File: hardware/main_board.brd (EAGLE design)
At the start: 91.4 x 66 mm, 108 parts, among them IC1 IC_USBLC6-2, IC2 LM1117IMPX-3.3, IC3 STM32F107RCT, IC4 DP83848, IC5 LM1117MPX-2.5, U1 USD-SOCKETUSD, U2 VS1003, X2 CRYSTALS-NOGND-CFPX-217, X3 KUSBVX, Y1 CRYSTAL-GROUNDEDSMD-5X3.2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

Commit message: minor changes
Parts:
- removed SV1: (no value), con-harting-ml:ML14L
- added SV2: (no value), con-harting-ml:ML10L
- moved C27 5.12 mm to (43.9, 10.8)
- moved C5 5.12 mm to (43.3, 8.92)
- moved IC1 5.12 mm to (48.3, 16.7)
- moved X3 5.12 mm to (48.3, 12.7)
- moved JP2 0.89 mm to (58.8, 6.39)
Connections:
- new net PA10: IC3.43, SV2.10
- new net PA8: IC3.41, SV2.8
- new net PA9: IC3.42, SV2.9
- new net PB14: IC3.35, SV2.2
- new net PB15: IC3.36, SV2.3
- new net PC6: IC3.37, SV2.4
- new net PC7: IC3.38, SV2.5
- new net PC8: IC3.39, SV2.6
- new net PC9: IC3.40, SV2.7
- net 3V: no longer SV1.1, SV1.2
- net GND: now also SV2.1; no longer SV1.3, SV1.4
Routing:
- net PB14: track 0.00 -> 19.0 mm
- net PC6: track 0.00 -> 18.3 mm
- net PC8: track 0.00 -> 17.7 mm
- net PA8: track 0.00 -> 17.0 mm
- net PA10: track 0.00 -> 16.4 mm
- net PB15: track 0.00 -> 15.6 mm
- net PC7: track 0.00 -> 14.9 mm
- net PC9: track 0.00 -> 14.3 mm
- net PA9: track 0.00 -> 13.7 mm
- net USB_P: track 8.27 -> 11.9 mm
- net USB_N: track 8.27 -> 11.9 mm
- net VBUS: track 89.9 -> 88.4 mm
- net 3V: track 442.8 -> 444.1 mm
- net SWD_CLK: track 29.5 -> 30.4 mm
- net NRST: track 56.0 -> 56.9 mm
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
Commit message: Minor changes
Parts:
- added C6: (no value), rcl:C0603
- added JP3: (no value), pinhead:1X02/90
- added R12: (no value), rcl:R0603
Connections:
- net 3V: now also JP3.1, R12.2
- net GND: now also C6.2, JP3.2
- net NRST: now also C6.1, R12.1
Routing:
- net 3V: track 444.1 -> 447.3 mm
- net NRST: track 56.9 -> 59.7 mm
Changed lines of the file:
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@@
 <setting verticaltext="up"/>
 </settings>
-<grid distance="25" unitdist="mil" unit="mil" style="lines" multiple="1" display="no" altdistance="1" altunitdist="mil" altunit="mil"/>
+<grid distance="25" unitdist="mil" unit="mil" style="lines" multiple="1" display="no" altdistance="5" altunitdist="mil" altunit="mil"/>
 <layers>
 <layer number="1" name="Top" color="4" fill="1" visible="yes" active="yes"/>
@@
 <attribute name="MF" value="" x="32.7406" y="10.795" size="1.778" layer="28" rot="MR180" display="off"/>
 </element>
+<element name="JP3" library="pinhead" package="1X02/90" value="" x="14.896221875" y="6.35" rot="MR180"/>
+<element name="R12" library="rcl" package="R0603" value="" x="50.8508" y="6.3872" rot="R180"/>
+<element name="C6" library="rcl" package="C0603" value="" x="53.7464" y="10.0584" rot="R90"/>
 </elements>
 <signals>
@@
 <via x="74.1934" y="8.4074" extent="1-16" drill="0.5" diameter="1.4224" shape="octagon"/>
 <wire x1="21.5794" y1="25.1108" x2="21.5794" y2="22.9616" width="0.3048" layer="1"/>
-<via x="6.0854" y="15.2654" extent="1-16" drill="0.6" diameter="1.4224" shape="octagon"/>
+<via x="6.0854" y="14.6304" extent="1-16" drill="0.6" diameter="1.4224" shape="octagon"/>
 <via x="26.2022" y="29.0068" extent="1-16" drill="0.6" diameter="1.4224" shape="octagon"/>
 <wire x1="21.0794" y1="33.4108" x2="21.0794" y2="30.6044" width="0.3048" layer="1"/>
@@
 <contactref element="SV2" pad="1"/>
 <via x="21.9604" y="14.6304" extent="1-16" drill="0.6" diameter="1.4224" shape="octagon"/>
+<contactref element="JP3" pad="2"/>
+<contactref element="C6" pad="2"/>
 </signal>
 <signal name="3V">
@@
 <wire x1="63.9064" y1="6.3872" x2="63.9064" y2="4.2164" width="1.016" layer="1"/>
 <wire x1="63.9064" y1="4.2164" x2="62.865" y2="3.175" width="1.016" layer="1"/>
-<wire x1="62.865" y1="3.175" x2="15.875" y2="3.175" width="1.016" layer="1"/>
+<wire x1="62.865" y1="3.175" x2="50.0008" y2="3.175" width="1.016" layer="1"/>
+<wire x1="50.0008" y1="3.175" x2="15.875" y2="3.175" width="1.016" layer="1"/>
 <wire x1="35.4488" y1="26.0108" x2="33.9598" y2="26.0108" width="0.3048" layer="1"/>
 <wire x1="33.9598" y1="26.0108" x2="33.9598" y2="25.81378125" width="0.3048" layer="1"/>
@@
 <wire x1="33.4614" y1="32.5108" x2="33.4614" y2="32.709090625" width="0.3048" layer="1"/>
 <wire x1="22.4926" y1="21.375" x2="24.0792" y2="22.9616" width="0.4064" layer="16"/>
+<wire x1="13.626221875" y1="5.423778125" x2="15.875" y2="3.175" width="1.016" layer="1"/>
+<contactref element="JP3" pad="1"/>
+<wire x1="13.626221875" y1="10.16" x2="13.626221875" y2="21.375" width="1.016" layer="1"/>
+<wire x1="13.626221875" y1="5.423778125" x2="13.626221875" y2="10.16" width="1.016" layer="1"/>
+<contactref element="R12" pad="2"/>
+<wire x1="50.0008" y1="6.3872" x2="50.0008" y2="3.175" width="0.6096" layer="1"/>
 <wire x1="13.626221875" y1="21.375" x2="22.4926" y2="21.375" width="0.4064" layer="16"/>
-<wire x1="15.875" y1="3.175" x2="13.626221875" y2="5.423778125" width="1.016" layer="1"/>
-<wire x1="13.626221875" y1="21.375" x2="13.626221875" y2="5.423778125" width="1.016" layer="1"/>
 <wire x1="25.5896" y1="41.43501875" x2="25.292559375" y2="41.43501875" width="0" layer="19" extent="1-1"/>
 </signal>
@@
 <contactref element="JP2" pad="5"/>
 <wire x1="58.5216" y1="17.6784" x2="57.1246" y2="19.0754" width="0.3048" layer="1"/>
-<wire x1="53.7464" y1="6.3872" x2="53.7464" y2="8.4328" width="0.3048" layer="1"/>
-<wire x1="53.7464" y1="8.4328" x2="58.5216" y2="13.208" width="0.3048" layer="1"/>
-<wire x1="58.5216" y1="17.6784" x2="58.5216" y2="13.208" width="0.3048" layer="1"/>
+<wire x1="55.03" y1="9.2084" x2="58.5216" y2="12.7" width="0.3048" layer="1"/>
+<wire x1="58.5216" y1="17.6784" x2="58.5216" y2="12.7" width="0.3048" layer="1"/>
 <via x="53.0098" y="19.0754" extent="1-16" drill="0.6" diameter="1.4224" shape="octagon"/>
 <wire x1="57.1246" y1="19.0754" x2="53.0098" y2="19.0754" width="0.3048" layer="1"/>
@@
 <wire x1="41.9488" y1="39.9662" x2="41.148" y2="40.767" width="0.3048" layer="16"/>
 <wire x1="42.8886" y1="31.115" x2="41.9488" y2="32.0548" width="0.3048" layer="16"/>
+<contactref element="R12" pad="1"/>
+<wire x1="51.7008" y1="6.3872" x2="53.7464" y2="6.3872" width="0.6096" layer="1"/>
+<contactref element="C6" pad="1"/>
+<wire x1="53.7464" y1="9.2084" x2="55.03" y2="9.2084" width="0.3048" layer="1"/>
+<wire x1="53.7464" y1="9.2084" x2="53.7464" y2="6.3872" width="0.6096" layer="1"/>
 </signal>
 <signal name="SWD_CLK">

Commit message: Minor changes
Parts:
- moved JP3 1.27 mm to (14.9, 7.62)
- moved R36 0.13 mm to (53.9, 38.5)
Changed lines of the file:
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@@
 <setting verticaltext="up"/>
 </settings>
-<grid distance="25" unitdist="mil" unit="mil" style="lines" multiple="1" display="no" altdistance="5" altunitdist="mil" altunit="mil"/>
+<grid distance="25" unitdist="mil" unit="mil" style="lines" multiple="1" display="no" altdistance="1" altunitdist="mil" altunit="mil"/>
 <layers>
 <layer number="1" name="Top" color="4" fill="1" visible="yes" active="yes"/>
@@
 <element name="L1" library="dp_devices" package="FB805" value="" x="73.025" y="42.291" rot="MR0"/>
 <element name="R35" library="rcl" package="R0603" value="" x="72.52461875" y="27.686"/>
-<element name="R36" library="rcl" package="R0603" value="100k" x="53.9242" y="38.3667" rot="R90"/>
+<element name="R36" library="rcl" package="R0603" value="100k" x="53.9242" y="38.4937" rot="R90"/>
 <element name="L2" library="dp_devices" package="FB805" value="" x="66.675" y="44.6786" rot="R180"/>
 <element name="C56" library="rcl" package="C0603" value="10 uF" x="68.4276" y="32.458659375" rot="R270"/>
@@
 <attribute name="MF" value="" x="32.7406" y="10.795" size="1.778" layer="28" rot="MR180" display="off"/>
 </element>
-<element name="JP3" library="pinhead" package="1X02/90" value="" x="14.896221875" y="6.35" rot="MR180"/>
+<element name="JP3" library="pinhead" package="1X02/90" value="" x="14.896221875" y="7.62" rot="MR180"/>
 <element name="R12" library="rcl" package="R0603" value="" x="50.8508" y="6.3872" rot="R180"/>
 <element name="C6" library="rcl" package="C0603" value="" x="53.7464" y="10.0584" rot="R90"/>
@@
 <via x="52.0192" y="64.516" extent="1-16" drill="0.5" diameter="1.27" shape="octagon"/>
 <via x="21.5794" y="22.9616" extent="1-16" drill="0.6" diameter="1.4224" shape="octagon"/>
-<via x="63.0428" y="36.4998" extent="1-16" drill="0.5" diameter="1.27" shape="octagon"/>
+<via x="63.4238" y="36.6014" extent="1-16" drill="0.5" diameter="1.27" shape="octagon"/>
 <contactref element="U2" pad="4"/>
 <contactref element="U2" pad="22"/>
@@
 <contactref element="IC3" pad="64"/>
 <contactref element="IC3" pad="48"/>
-<via x="61.214" y="36.5506" extent="1-16" drill="0.6" diameter="1.4224" shape="octagon"/>
-<wire x1="61.214" y1="36.5506" x2="61.214" y2="33.308659375" width="1.016" layer="16"/>
+<via x="61.214" y="36.6776" extent="1-16" drill="0.6" diameter="1.4224" shape="octagon"/>
+<wire x1="61.214" y1="36.6776" x2="61.214" y2="33.308659375" width="1.016" layer="16"/>
 <wire x1="44.9488" y1="32.8758" x2="44.9488" y2="26.0108" width="0.3048" layer="1"/>
 <wire x1="44.9488" y1="26.0108" x2="44.9488" y2="24.0108" width="0.3048" layer="1"/>
@@
 <wire x1="64.71181875" y1="40.382" x2="61.591" y2="40.382" width="0.254" layer="1"/>
 <wire x1="61.591" y1="40.382" x2="61.214" y2="40.005" width="0.254" layer="1"/>
-<wire x1="61.214" y1="40.005" x2="61.214" y2="36.5506" width="0.254" layer="1"/>
-<wire x1="61.214" y1="36.5506" x2="52.4764" y2="36.5506" width="0.3048" layer="1"/>
-<wire x1="51.8922" y1="35.9664" x2="52.4764" y2="36.5506" width="0.3048" layer="1"/>
+<wire x1="61.214" y1="40.005" x2="61.214" y2="36.6776" width="0.254" layer="1"/>
+<wire x1="51.8922" y1="35.9664" x2="52.6034" y2="36.6776" width="0.3048" layer="1"/>
 <wire x1="48.80101875" y1="33.5108" x2="48.80101875" y2="33.71111875" width="0.3048" layer="1"/>
 <wire x1="48.80101875" y1="33.5108" x2="51.5194" y2="33.5108" width="0.3048" layer="1"/>
 <wire x1="51.5194" y1="33.5108" x2="51.8922" y2="33.8836" width="0.3048" layer="1"/>
 <wire x1="51.8922" y1="35.9664" x2="51.8922" y2="33.8836" width="0.3048" layer="1"/>
-<wire x1="61.214" y1="36.5506" x2="61.214" y2="62.46" width="1.016" layer="16"/>
+<wire x1="61.214" y1="36.6776" x2="61.214" y2="62.46" width="1.016" layer="16"/>
 <wire x1="61.214" y1="62.46" x2="61.214" y2="60.3518" width="1.016" layer="1"/>
 <wire x1="61.214" y1="60.3518" x2="61.1632" y2="60.301" width="1.016" layer="1"/>
@@
 <wire x1="13.626221875" y1="5.423778125" x2="15.875" y2="3.175" width="1.016" layer="1"/>
 <contactref element="JP3" pad="1"/>
-<wire x1="13.626221875" y1="10.16" x2="13.626221875" y2="21.375" width="1.016" layer="1"/>
-<wire x1="13.626221875" y1="5.423778125" x2="13.626221875" y2="10.16" width="1.016" layer="1"/>
+<wire x1="13.626221875" y1="11.43" x2="13.626221875" y2="21.375" width="1.016" layer="1"/>
+<wire x1="13.626221875" y1="5.423778125" x2="13.626221875" y2="11.43" width="1.016" layer="1"/>
 <contactref element="R12" pad="2"/>
 <wire x1="50.0008" y1="6.3872" x2="50.0008" y2="3.175" width="0.6096" layer="1"/>
 <wire x1="13.626221875" y1="21.375" x2="22.4926" y2="21.375" width="0.4064" layer="16"/>
+<wire x1="61.214" y1="36.6776" x2="52.6034" y2="36.6776" width="0.3048" layer="1"/>
 <wire x1="25.5896" y1="41.43501875" x2="25.292559375" y2="41.43501875" width="0" layer="19" extent="1-1"/>
 </signal>
@@
 <wire x1="67.8968" y1="41.882" x2="66.4972" y2="43.2816" width="0.254" layer="1"/>
 <wire x1="44.4488" y1="35.5108" x2="44.4488" y2="36.4986" width="0.254" layer="1"/>
-<wire x1="44.4488" y1="36.4986" x2="45.085" y2="37.1348" width="0.254" layer="1"/>
-<wire x1="45.085" y1="37.1348" x2="53.975" y2="37.1348" width="0.254" layer="1"/>
-<wire x1="53.975" y1="37.1348" x2="60.1726" y2="37.1348" width="0.254" layer="1"/>
-<wire x1="60.1726" y1="37.1348" x2="60.6552" y2="37.6174" width="0.254" layer="1"/>
-<wire x1="60.6552" y1="37.6174" x2="60.6552" y2="42.4688" width="0.254" layer="1"/>
+<wire x1="44.4488" y1="36.4986" x2="45.212" y2="37.2618" width="0.254" layer="1"/>
+<wire x1="60.6552" y1="37.7444" x2="60.6552" y2="42.4688" width="0.254" layer="1"/>
 <wire x1="60.6552" y1="42.4688" x2="61.468" y2="43.2816" width="0.254" layer="1"/>
 <wire x1="66.4972" y1="43.2816" x2="61.468" y2="43.2816" width="0.254" layer="1"/>
-<wire x1="53.9242" y1="37.5167" x2="53.9242" y2="37.1856" width="0.254" layer="1"/>
-<wire x1="53.9242" y1="37.1856" x2="53.975" y2="37.1348" width="0.254" layer="1"/>
+<wire x1="60.6552" y1="37.7444" x2="60.1726" y2="37.2618" width="0.254" layer="1"/>
+<wire x1="60.1726" y1="37.2618" x2="53.975" y2="37.2618" width="0.254" layer="1"/>
+<wire x1="53.975" y1="37.2618" x2="45.212" y2="37.2618" width="0.254" layer="1"/>
+<wire x1="53.9242" y1="37.6437" x2="53.9242" y2="37.3126" width="0.254" layer="1"/>
+<wire x1="53.9242" y1="37.3126" x2="53.975" y2="37.2618" width="0.254" layer="1"/>
 </signal>
 <signal name="VS_MISO">
@@
 <wire x1="75.0062" y1="37.4904" x2="70.358" y2="37.4904" width="0.254" layer="1"/>
 <wire x1="70.358" y1="37.4904" x2="69.6976" y2="36.83" width="0.254" layer="1"/>
-<wire x1="69.6976" y1="36.83" x2="69.6976" y2="35.5092" width="0.254" layer="1"/>
+<wire x1="69.6976" y1="36.83" x2="69.6976" y2="35.56" width="0.254" layer="1"/>
 <contactref element="IC3" pad="59"/>
-<wire x1="46.9488" y1="31.0108" x2="56.5632" y2="31.0108" width="0.254" layer="1"/>
-<wire x1="69.6976" y1="35.5092" x2="69.1134" y2="34.925" width="0.254" layer="1"/>
-<wire x1="69.1134" y1="34.925" x2="60.4774" y2="34.925" width="0.254" layer="1"/>
-<wire x1="56.5632" y1="31.0108" x2="60.4774" y2="34.925" width="0.254" layer="1"/>
+<wire x1="46.9488" y1="31.0108" x2="56.487" y2="31.0108" width="0.254" layer="1"/>
+<wire x1="69.6976" y1="35.56" x2="69.1134" y2="34.9758" width="0.254" layer="1"/>
+<wire x1="56.487" y1="31.0108" x2="60.452" y2="34.9758" width="0.254" layer="1"/>
+<wire x1="60.452" y1="34.9758" x2="69.1134" y2="34.9758" width="0.254" layer="1"/>
 </signal>
 <signal name="VS_DREQ">
@@
 <wire x1="68.775" y1="39.382" x2="65.0868" y2="39.382" width="0.254" layer="1"/>
 <contactref element="IC3" pad="61"/>
-<wire x1="46.9488" y1="32.0108" x2="56.852" y2="32.0108" width="0.254" layer="1"/>
+<wire x1="46.9488" y1="32.0108" x2="56.6996" y2="32.0108" width="0.254" layer="1"/>
 <wire x1="65.0868" y1="39.382" x2="64.897" y2="39.1922" width="0.254" layer="1"/>
-<wire x1="64.897" y1="39.1922" x2="64.897" y2="35.7124" width="0.254" layer="1"/>
-<wire x1="64.897" y1="35.7124" x2="64.6176" y2="35.433" width="0.254" layer="1"/>
-<wire x1="64.6176" y1="35.433" x2="60.2742" y2="35.433" width="0.254" layer="1"/>
-<wire x1="60.2742" y1="35.433" x2="56.852" y2="32.0108" width="0.254" layer="1"/>
+<wire x1="64.897" y1="39.1922" x2="64.897" y2="35.814" width="0.254" layer="1"/>
+<wire x1="64.897" y1="35.814" x2="64.6176" y2="35.5346" width="0.254" layer="1"/>
+<wire x1="64.6176" y1="35.5346" x2="60.2234" y2="35.5346" width="0.254" layer="1"/>
+<wire x1="56.6996" y1="32.0108" x2="60.2234" y2="35.5346" width="0.254" layer="1"/>
 </signal>
 <signal name="VS_XDCS">

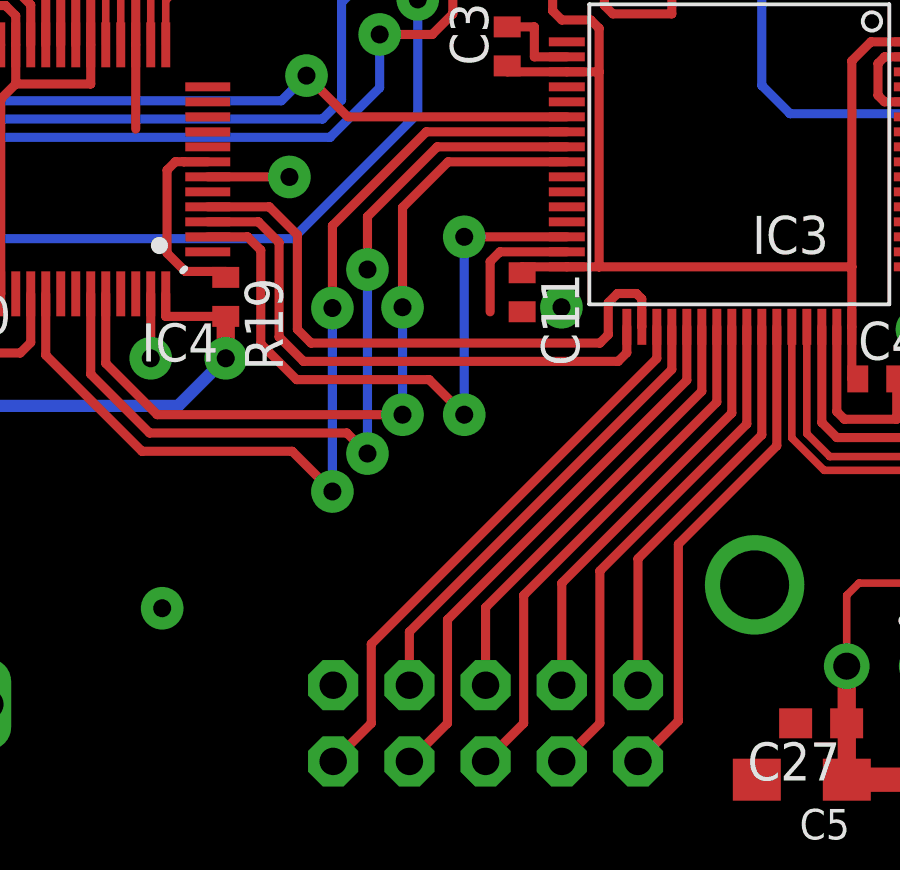
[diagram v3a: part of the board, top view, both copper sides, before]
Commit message: UART3 TX trace added
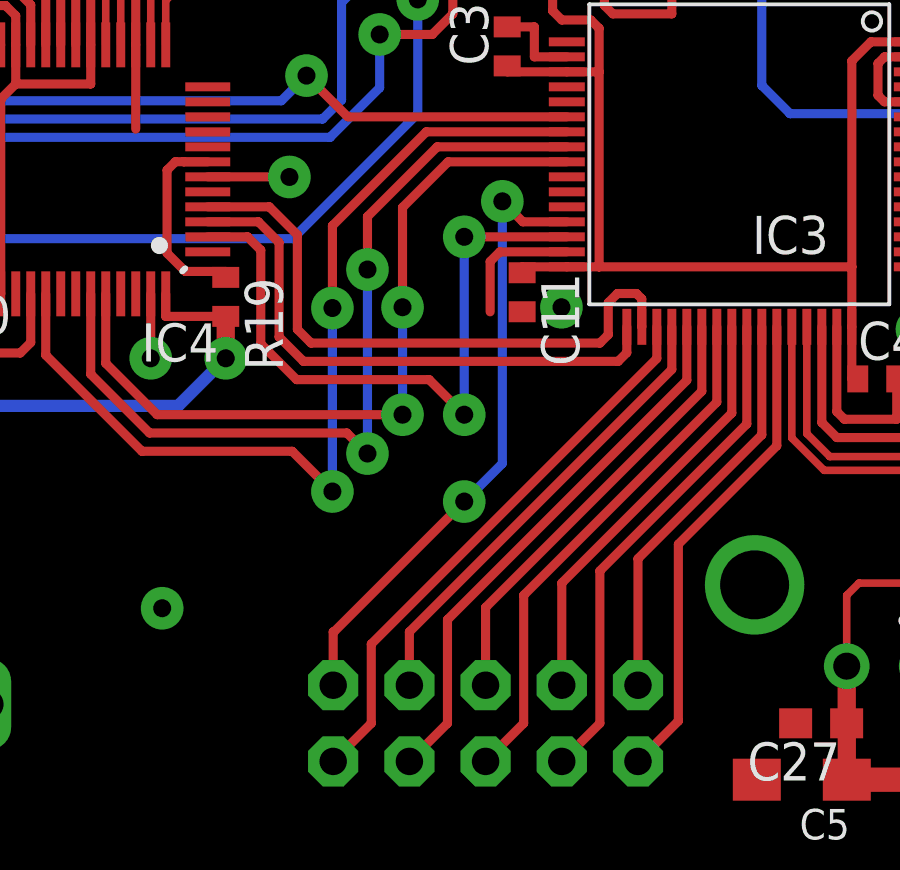
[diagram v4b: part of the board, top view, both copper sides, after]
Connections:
- new net UART_TX: IC3.29, SV2.1
- net GND: no longer SV2.1
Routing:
- net UART_TX: track 0.00 -> 20.9 mm, vias 0 -> 2
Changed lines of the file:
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@@
 <setting verticaltext="up"/>
 </settings>
-<grid distance="25" unitdist="mil" unit="mil" style="lines" multiple="1" display="no" altdistance="1" altunitdist="mil" altunit="mil"/>
+<grid distance="25" unitdist="mil" unit="mil" style="lines" multiple="1" display="no" altdistance="5" altunitdist="mil" altunit="mil"/>
 <layers>
 <layer number="1" name="Top" color="4" fill="1" visible="yes" active="yes"/>
@@
 <wire x1="38.1" y1="40.132" x2="38.1762" y2="40.132" width="0.3048" layer="1"/>
 <via x="26.0324" y="35.814" extent="1-16" drill="0.6" diameter="1.4224" shape="octagon"/>
-<contactref element="SV2" pad="1"/>
 <via x="21.9604" y="14.6304" extent="1-16" drill="0.6" diameter="1.4224" shape="octagon"/>
 <contactref element="JP3" pad="2"/>
@@
 <contactref element="SV2" pad="9"/>
 </signal>
+<signal name="UART_TX">
+<contactref element="IC3" pad="29"/>
+<contactref element="SV2" pad="1"/>
+<via x="33.2994" y="28.194" extent="1-16" drill="0.6" diameter="1.4224" shape="octagon"/>
+<wire x1="35.4488" y1="27.5108" x2="33.9826" y2="27.5108" width="0.3048" layer="1"/>
+<wire x1="33.9826" y1="27.5108" x2="33.2994" y2="28.194" width="0.3048" layer="1"/>
+<via x="32.0294" y="18.1864" extent="1-16" drill="0.6" diameter="1.4224" shape="octagon"/>
+<wire x1="27.6606" y1="12.065" x2="27.6606" y2="13.843" width="0.3048" layer="1"/>
+<wire x1="27.6606" y1="13.843" x2="27.686" y2="13.843" width="0.3048" layer="1"/>
+<wire x1="27.686" y1="13.843" x2="32.0294" y2="18.1864" width="0.3048" layer="1"/>
+<wire x1="33.2994" y1="28.194" x2="33.2994" y2="19.4564" width="0.3048" layer="16"/>
+<wire x1="33.2994" y1="19.4564" x2="32.0294" y2="18.1864" width="0.3048" layer="16"/>
+</signal>
 </signals>
